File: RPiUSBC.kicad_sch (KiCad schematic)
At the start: 0 parts

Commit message: Fixed Merge Conflicts
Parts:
- added U4: CH224K, Package_SO:SSOP-10-1EP_3.9x4.9mm_P1mm_EP2.1x3.3mm, symbol Interface_USB:CH224K
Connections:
- new net GND: U4.11 (GND)
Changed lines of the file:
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@@
 	(generator_version "9.0")
 	(paper "A4")
+	(wire
+		(pts
+			(xy 96.52 120.65) (xy 96.52 130.81)
+		)
+		(stroke
+			(width 0)
+			(type default)
+		)
+	)
+	(symbol
+		(lib_id "power:GND")
+		(at 96.52 130.81 0)
+		(unit 1)
+		(exclude_from_sim no)
+		(in_bom yes)
+		(on_board yes)
+		(dnp no)
+		(fields_autoplaced yes)
+		(property "Reference" "#PWR08"
+			(at 96.52 137.16 0)
+			(effects
+				(font
+					(size 1.27 1.27)
+				)
+				(hide yes)
+			)
+		)
+		(property "Value" "GND"
+			(at 96.52 135.89 0)
+			(effects
+				(font
+					(size 1.27 1.27)
+				)
+			)
+		)
+		(property "Footprint" ""
+			(at 96.52 130.81 0)
+			(effects
+				(font
+					(size 1.27 1.27)
+				)
+				(hide yes)
+			)
+		)
+		(property "Datasheet" ""
+			(at 96.52 130.81 0)
+			(effects
+				(font
+					(size 1.27 1.27)
+				)
+				(hide yes)
+			)
+		)
+		(property "Description" "Power symbol creates a global label with name \"GND\" , ground"
+			(at 96.52 130.81 0)
+			(effects
+				(font
+					(size 1.27 1.27)
+				)
+				(hide yes)
+			)
+		)
+		(pin "1"
+		)
+		(instances
+			(project ""
+				(path "/74aeb085-833c-4e9c-940c-e21ceb3a8c2a"
+					(reference "#PWR01")
+					(unit 1)
+				)
+			)
+			(project "PAFT_pcbs"
+				(path "/8372e765-ead7-42d0-82da-59a3937ad504/44926947-e48e-4e04-bb40-de8c52f1099b"
+					(reference "#PWR08")
+					(unit 1)
+				)
+			)
+		)
+	)
+	(symbol
+		(lib_id "Interface_USB:CH224K")
+		(at 96.52 110.49 0)
+		(unit 1)
+		(exclude_from_sim no)
+		(in_bom yes)
+		(on_board yes)
+		(dnp no)
+		(fields_autoplaced yes)
+		(property "Reference" "U4"
+			(at 98.6633 120.65 0)
+			(effects
+				(font
+					(size 1.27 1.27)
+				)
+				(justify left)
+			)
+		)
+		(property "Value" "CH224K"
+			(at 98.6633 123.19 0)
+			(effects
+				(font
+					(size 1.27 1.27)
+				)
+				(justify left)
+			)
+		)
+		(property "Footprint" "Package_SO:SSOP-10-1EP_3.9x4.9mm_P1mm_EP2.1x3.3mm"
+			(at 96.52 134.62 0)
+			(effects
+				(font
+					(size 1.27 1.27)
+				)
+				(hide yes)
+			)
+		)
+		(property "Datasheet" "https://www.wch.cn/downloads/file/301.html"
+			(at 96.52 96.52 0)
+			(effects
+				(font
+					(size 1.27 1.27)
+				)
+				(hide yes)
+			)
+		)
+		(property "Description" "100W USB Type-C PD3.0/2.0, BC1.2 Sink Controller, SSOP-10"
+			(at 96.52 110.49 0)
+			(effects
+				(font
+					(size 1.27 1.27)
+				)
+				(hide yes)
+			)
+		)
+		(pin "6"
+		)
+		(pin "7"
+		)
+		(pin "5"
+		)
+		(pin "4"
+		)
+		(pin "8"
+		)
+		(pin "11"
+		)
+		(pin "1"
+		)
+		(pin "10"
+		)
+		(pin "9"
+		)
+		(pin "2"
+		)
+		(pin "3"
+		)
+		(instances
+			(project ""
+				(path "/74aeb085-833c-4e9c-940c-e21ceb3a8c2a"
+					(reference "U1")
+					(unit 1)
+				)
+			)
+			(project "PAFT_pcbs"
+				(path "/8372e765-ead7-42d0-82da-59a3937ad504/44926947-e48e-4e04-bb40-de8c52f1099b"
+					(reference "U4")
+					(unit 1)
+				)
+			)
+		)
+	)
+	(sheet_instances
+		(path "/"
+			(page "1")
+		)
+	)
+	(embedded_fonts no)
 )

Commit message: Revert "Fixed Merge Conflicts"
This reverts commit 1dcac9fe20d43ad9866d81964f948f071540213e.
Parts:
- removed U4: CH224K, Package_SO:SSOP-10-1EP_3.9x4.9mm_P1mm_EP2.1x3.3mm, symbol Interface_USB:CH224K
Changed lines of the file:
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@@
 	(generator_version "9.0")
 	(paper "A4")
-	(wire
-		(pts
-			(xy 96.52 120.65) (xy 96.52 130.81)
-		)
-		(stroke
-			(width 0)
-			(type default)
-		)
-	)
-	(symbol
-		(lib_id "power:GND")
-		(at 96.52 130.81 0)
-		(unit 1)
-		(exclude_from_sim no)
-		(in_bom yes)
-		(on_board yes)
-		(dnp no)
-		(fields_autoplaced yes)
-		(property "Reference" "#PWR08"
-			(at 96.52 137.16 0)
-			(effects
-				(font
-					(size 1.27 1.27)
-				)
-				(hide yes)
-			)
-		)
-		(property "Value" "GND"
-			(at 96.52 135.89 0)
-			(effects
-				(font
-					(size 1.27 1.27)
-				)
-			)
-		)
-		(property "Footprint" ""
-			(at 96.52 130.81 0)
-			(effects
-				(font
-					(size 1.27 1.27)
-				)
-				(hide yes)
-			)
-		)
-		(property "Datasheet" ""
-			(at 96.52 130.81 0)
-			(effects
-				(font
-					(size 1.27 1.27)
-				)
-				(hide yes)
-			)
-		)
-		(property "Description" "Power symbol creates a global label with name \"GND\" , ground"
-			(at 96.52 130.81 0)
-			(effects
-				(font
-					(size 1.27 1.27)
-				)
-				(hide yes)
-			)
-		)
-		(pin "1"
-		)
-		(instances
-			(project ""
-				(path "/74aeb085-833c-4e9c-940c-e21ceb3a8c2a"
-					(reference "#PWR01")
-					(unit 1)
-				)
-			)
-			(project "PAFT_pcbs"
-				(path "/8372e765-ead7-42d0-82da-59a3937ad504/44926947-e48e-4e04-bb40-de8c52f1099b"
-					(reference "#PWR08")
-					(unit 1)
-				)
-			)
-		)
-	)
-	(symbol
-		(lib_id "Interface_USB:CH224K")
-		(at 96.52 110.49 0)
-		(unit 1)
-		(exclude_from_sim no)
-		(in_bom yes)
-		(on_board yes)
-		(dnp no)
-		(fields_autoplaced yes)
-		(property "Reference" "U4"
-			(at 98.6633 120.65 0)
-			(effects
-				(font
-					(size 1.27 1.27)
-				)
-				(justify left)
-			)
-		)
-		(property "Value" "CH224K"
-			(at 98.6633 123.19 0)
-			(effects
-				(font
-					(size 1.27 1.27)
-				)
-				(justify left)
-			)
-		)
-		(property "Footprint" "Package_SO:SSOP-10-1EP_3.9x4.9mm_P1mm_EP2.1x3.3mm"
-			(at 96.52 134.62 0)
-			(effects
-				(font
-					(size 1.27 1.27)
-				)
-				(hide yes)
-			)
-		)
-		(property "Datasheet" "https://www.wch.cn/downloads/file/301.html"
-			(at 96.52 96.52 0)
-			(effects
-				(font
-					(size 1.27 1.27)
-				)
-				(hide yes)
-			)
-		)
-		(property "Description" "100W USB Type-C PD3.0/2.0, BC1.2 Sink Controller, SSOP-10"
-			(at 96.52 110.49 0)
-			(effects
-				(font
-					(size 1.27 1.27)
-				)
-				(hide yes)
-			)
-		)
-		(pin "6"
-		)
-		(pin "7"
-		)
-		(pin "5"
-		)
-		(pin "4"
-		)
-		(pin "8"
-		)
-		(pin "11"
-		)
-		(pin "1"
-		)
-		(pin "10"
-		)
-		(pin "9"
-		)
-		(pin "2"
-		)
-		(pin "3"
-		)
-		(instances
-			(project ""
-				(path "/74aeb085-833c-4e9c-940c-e21ceb3a8c2a"
-					(reference "U1")
-					(unit 1)
-				)
-			)
-			(project "PAFT_pcbs"
-				(path "/8372e765-ead7-42d0-82da-59a3937ad504/44926947-e48e-4e04-bb40-de8c52f1099b"
-					(reference "U4")
-					(unit 1)
-				)
-			)
-		)
-	)
-	(sheet_instances
-		(path "/"
-			(page "1")
-		)
-	)
-	(embedded_fonts no)
 )

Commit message: Added voltage/signal test points
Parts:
- added J7: USB_C_Receptacle_PowerOnly_6P, symbol Connector:USB_C_Receptacle_PowerOnly_6P
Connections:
- new net +12V: J7.A9 (VBUS), J7.B9 (VBUS)
- new net GND: J7.A12 (GND), J7.B12 (GND), J7.S1 (SHIELD)

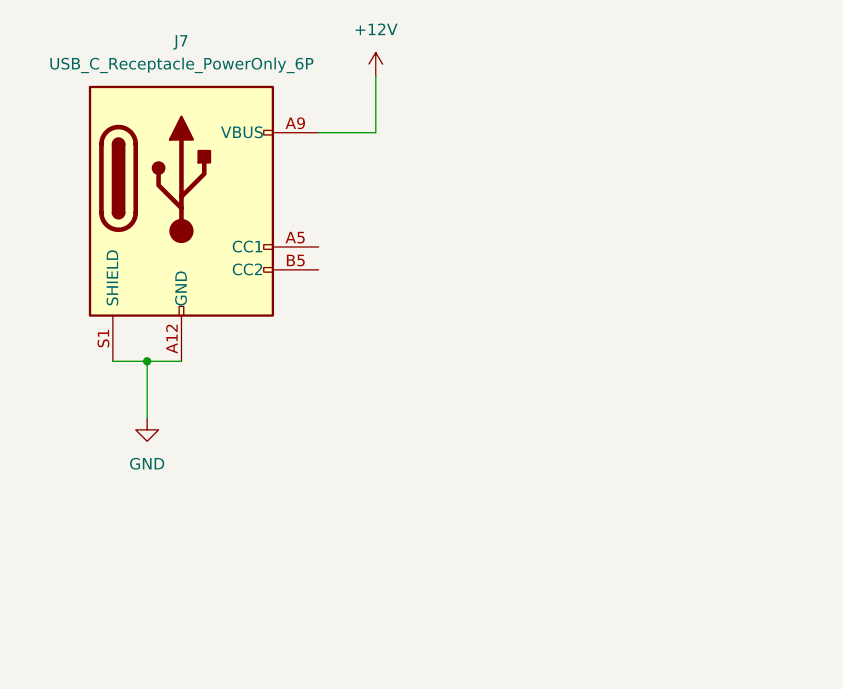
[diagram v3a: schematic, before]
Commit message: USB C IC added
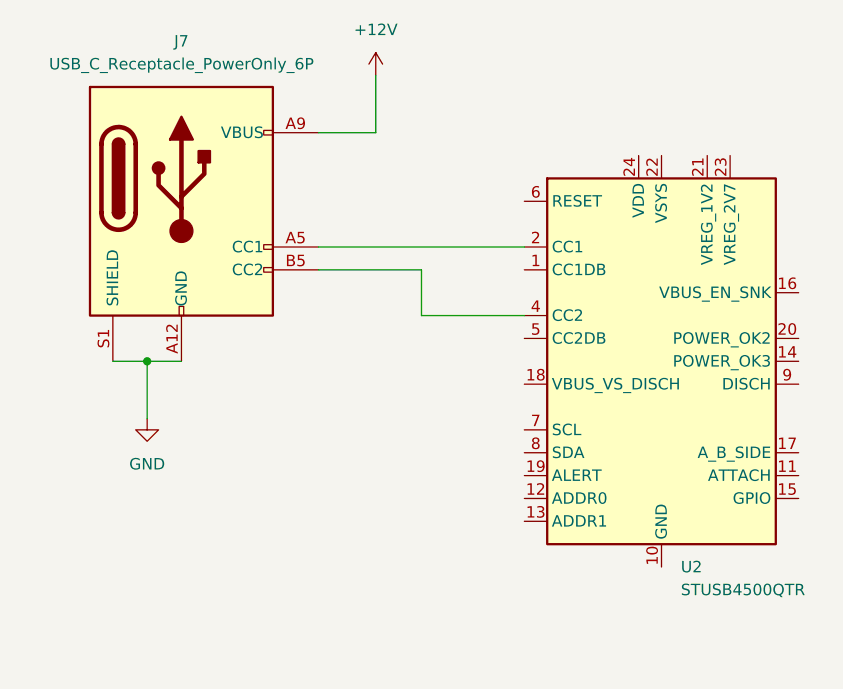
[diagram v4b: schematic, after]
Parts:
- added U2: STUSB4500QTR, Package_DFN_QFN:QFN-24-1EP_4x4mm_P0.5mm_EP2.7x2.7mm, symbol Interface_USB:STUSB4500QTR
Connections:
- net at J7.A5 (CC1): now also U2.2 (CC1)
- net at J7.B5 (CC2): now also U2.4 (CC2)
- new net: U2.10 (GND), U2.25 (GND)
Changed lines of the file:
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@@
+	(wire
+		(pts
+			(xy 127 97.79) (xy 127 92.71)
+		)
+		(stroke
+			(width 0)
+			(type default)
+		)
+	)
 	(wire
 		(pts
@@
 	(wire
 		(pts
+			(xy 115.57 90.17) (xy 138.43 90.17)
+		)
+		(stroke
+			(width 0)
+			(type default)
+		)
+	)
+	(wire
+		(pts
 			(xy 92.71 102.87) (xy 96.52 102.87)
+		)
+		(stroke
+			(width 0)
+			(type default)
+		)
+	)
+	(wire
+		(pts
+			(xy 138.43 97.79) (xy 127 97.79)
+		)
+		(stroke
+			(width 0)
+			(type default)
+		)
+	)
+	(wire
+		(pts
+			(xy 127 92.71) (xy 115.57 92.71)
 		)
 		(stroke
@@
 					(unit 1)
 				)
+			)
+		)
+	)
+	(symbol
+		(lib_id "Interface_USB:STUSB4500QTR")
+		(at 153.67 102.87 0)
+		(unit 1)
+		(exclude_from_sim no)
+		(in_bom yes)
+		(on_board yes)
+		(dnp no)
+		(fields_autoplaced yes)
+		(property "Reference" "U2"
+			(at 155.8133 125.73 0)
+			(effects
+				(font
+					(size 1.27 1.27)
+				)
+				(justify left)
+			)
+		)
+		(property "Value" "STUSB4500QTR"
+			(at 155.8133 128.27 0)
+			(effects
+				(font
+					(size 1.27 1.27)
+				)
+				(justify left)
+			)
+		)
+		(property "Footprint" "Package_DFN_QFN:QFN-24-1EP_4x4mm_P0.5mm_EP2.7x2.7mm"
+			(at 153.67 102.87 0)
+			(effects
+				(font
+					(size 1.27 1.27)
+				)
+				(hide yes)
+			)
+		)
+		(property "Datasheet" "https://www.st.com/resource/en/datasheet/stusb4500.pdf"
+			(at 153.67 102.87 0)
+			(effects
+				(font
+					(size 1.27 1.27)
+				)
+				(hide yes)
+			)
+		)
+		(property "Description" "Stand-alone USB PD controller (with sink Auto-run mode), QFN-24"
+			(at 153.67 102.87 0)
+			(effects
+				(font
+					(size 1.27 1.27)
+				)
+				(hide yes)
+			)
+		)
+		(pin "6"
+		)
+		(pin "2"
+		)
+		(pin "18"
+		)
+		(pin "12"
+		)
+		(pin "24"
+		)
+		(pin "19"
+		)
+		(pin "10"
+		)
+		(pin "3"
+		)
+		(pin "13"
+		)
+		(pin "4"
+		)
+		(pin "7"
+		)
+		(pin "8"
+		)
+		(pin "22"
+		)
+		(pin "5"
+		)
+		(pin "1"
+		)
+		(pin "14"
+		)
+		(pin "23"
+		)
+		(pin "20"
+		)
+		(pin "11"
+		)
+		(pin "25"
+		)
+		(pin "16"
+		)
+		(pin "21"
+		)
+		(pin "9"
+		)
+		(pin "17"
+		)
+		(pin "15"
+		)
+		(instances
+			(project ""
+				(path "/8372e765-ead7-42d0-82da-59a3937ad504/44926947-e48e-4e04-bb40-de8c52f1099b"
+					(reference "U2")
+					(unit 1)
+				)
